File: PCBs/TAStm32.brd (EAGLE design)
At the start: 45 x 68.1 mm, 23 parts, among them J1 ZX62D-B-5PA8, P1 RJHSE-5381, P1_DEBUG 6_PIN_SERIAL_CABLEPTH, P2 RJHSE-5381, P2_DEBUG 6_PIN_SERIAL_CABLEPTH, U1 STM32F446RET6

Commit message: updated PCBs to v1
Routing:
- net N$3: track 19.8 -> 17.4 mm, vias 2 -> 0
- net V2_D0: track 27.0 -> 29.3 mm
- net V2_LATCH: track 31.2 -> 33.4 mm
- net V2_CLOCK: track 33.5 -> 35.5 mm
- net V2_D1: track 30.7 -> 32.7 mm
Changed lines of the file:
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@@
 <text x="14.3" y="20.4" size="0.6096" layer="25" font="vector" ratio="15" rot="R180">SWITCH</text>
 <text x="10" y="34" size="0.6096" layer="25" font="vector" ratio="15">V_REG</text>
-<text x="28.9" y="25.7" size="0.6096" layer="26" font="vector" ratio="15" rot="MR0">Hardware design by:
+<text x="24.9" y="21.7" size="0.6096" layer="26" font="vector" ratio="15" rot="MR0">Hardware design by:
 Ownasaurus
 https://github.com/Ownasaurus/TAStm32</text>
@@
 <contactref element="R2" pad="2"/>
 <contactref element="SWITCH" pad="P$2"/>
-<wire x1="17.24" y1="20.03" x2="20" y2="20.03" width="0.1524" layer="1"/>
-<wire x1="20" y1="20.03" x2="20" y2="20" width="0.1524" layer="1"/>
-<via x="20" y="20" extent="1-16" drill="0.35"/>
-<wire x1="20" y1="20" x2="20" y2="23" width="0.1524" layer="16"/>
-<via x="20" y="23" extent="1-16" drill="0.35"/>
-<wire x1="20" y1="23" x2="18.17" y2="24.83" width="0.1524" layer="1"/>
-<wire x1="18.17" y1="24.83" x2="17.47" y2="24.83" width="0.1524" layer="1"/>
-<wire x1="28.8786" y1="24.93368125" x2="28.70368125" y2="25.1086" width="0.1524" layer="1"/>
+<wire x1="28.70368125" y1="25.1086" x2="28.8786" y2="24.93368125" width="0.1524" layer="1"/>
 <wire x1="29.01" y1="24.1" x2="28.8786" y2="24.2314" width="0.1524" layer="1"/>
 <wire x1="28.8786" y1="24.2314" x2="28.8786" y2="24.93368125" width="0.1524" layer="1"/>
-<wire x1="28.70368125" y1="25.1086" x2="22.1086" y2="25.1086" width="0.1524" layer="1"/>
-<wire x1="22.1086" y1="25.1086" x2="20" y2="23" width="0.1524" layer="1"/>
+<wire x1="17.24" y1="20.03" x2="17.24" y2="24.6" width="0.1524" layer="1"/>
+<wire x1="17.24" y1="24.6" x2="17.47" y2="24.83" width="0.1524" layer="1"/>
+<wire x1="17.47" y1="24.83" x2="17.7486" y2="25.1086" width="0.1524" layer="1"/>
+<wire x1="17.7486" y1="25.1086" x2="28.70368125" y2="25.1086" width="0.1524" layer="1"/>
 </signal>
 <signal name="N$4">
@@
 <wire x1="5.0436" y1="10.7657125" x2="5" y2="10.7221125" width="0.1524" layer="1"/>
 <wire x1="5" y1="10.7221125" x2="5" y2="8.76" width="0.1524" layer="1"/>
-<wire x1="24.01" y1="24.1" x2="23.8786" y2="23.9686" width="0.1524" layer="1"/>
-<wire x1="23.8786" y1="23.9686" x2="23.8786" y2="23.26631875" width="0.1524" layer="1"/>
-<wire x1="23.8786" y1="23.26631875" x2="22.61228125" y2="22" width="0.1524" layer="1"/>
-<wire x1="22.61228125" y1="22" x2="15" y2="22" width="0.1524" layer="1"/>
-<wire x1="15" y1="22" x2="11" y2="18" width="0.1524" layer="1"/>
-<wire x1="11" y1="18" x2="7" y2="18" width="0.1524" layer="1"/>
-<wire x1="7" y1="18" x2="5" y2="16" width="0.1524" layer="1"/>
-<wire x1="5" y1="16" x2="5" y2="15" width="0.1524" layer="1"/>
+<wire x1="5" y1="15" x2="8.3048" y2="18.3048" width="0.1524" layer="1"/>
+<wire x1="8.3048" y1="18.3048" x2="23.4" y2="18.3048" width="0.1524" layer="1"/>
+<wire x1="23.4" y1="18.3048" x2="24.01" y2="18.9148" width="0.1524" layer="1"/>
+<wire x1="24.01" y1="18.9148" x2="24.01" y2="24.1" width="0.1524" layer="1"/>
 </signal>
 <signal name="V2_LATCH">
@@
 <wire x1="7.54" y1="15" x2="7.54" y2="8.25" width="0.1524" layer="1"/>
 <wire x1="7.54" y1="8.25" x2="9.47" y2="6.32" width="0.1524" layer="1"/>
-<wire x1="7.54" y1="15" x2="9.54" y2="17" width="0.1524" layer="1"/>
-<wire x1="9.54" y1="17" x2="12" y2="17" width="0.1524" layer="1"/>
-<wire x1="12" y1="17" x2="16" y2="21" width="0.1524" layer="1"/>
-<wire x1="16" y1="21" x2="23" y2="21" width="0.1524" layer="1"/>
-<wire x1="23" y1="21" x2="24.51" y2="22.51" width="0.1524" layer="1"/>
-<wire x1="24.51" y1="22.51" x2="24.51" y2="24.1" width="0.1524" layer="1"/>
+<wire x1="7.54" y1="15" x2="10.54" y2="18" width="0.1524" layer="1"/>
+<wire x1="10.54" y1="18" x2="23.9" y2="18" width="0.1524" layer="1"/>
+<wire x1="23.9" y1="18" x2="24.51" y2="18.61" width="0.1524" layer="1"/>
+<wire x1="24.51" y1="18.61" x2="24.51" y2="24.1" width="0.1524" layer="1"/>
 </signal>
 <signal name="V2_D1">
@@
 <wire x1="10.49" y1="4.54" x2="10.49" y2="14.59" width="0.1524" layer="1"/>
 <wire x1="10.49" y1="14.59" x2="10.08" y2="15" width="0.1524" layer="1"/>
-<wire x1="25.01" y1="24.1" x2="25" y2="24.09" width="0.1524" layer="1"/>
-<wire x1="25" y1="24.09" x2="25" y2="22" width="0.1524" layer="1"/>
-<wire x1="25" y1="22" x2="22" y2="19" width="0.1524" layer="1"/>
-<wire x1="12.4" y1="16.4" x2="11.2" y2="16.4" width="0.1524" layer="1"/>
-<wire x1="11.2" y1="16.4" x2="10.08" y2="15.28" width="0.1524" layer="1"/>
-<wire x1="10.08" y1="15.28" x2="10.08" y2="15" width="0.1524" layer="1"/>
-<wire x1="22" y1="19" x2="15" y2="19" width="0.1524" layer="1"/>
-<wire x1="15" y1="19" x2="12.4" y2="16.4" width="0.1524" layer="1"/>
+<wire x1="25" y1="24.09" x2="25.01" y2="24.1" width="0.1524" layer="1"/>
+<wire x1="10.08" y1="15" x2="12.3848" y2="17.3048" width="0.1524" layer="1"/>
+<wire x1="12.3848" y1="17.3048" x2="24" y2="17.3048" width="0.1524" layer="1"/>
+<wire x1="24" y1="17.3048" x2="25" y2="18.3048" width="0.1524" layer="1"/>
+<wire x1="25" y1="18.3048" x2="25" y2="24.09" width="0.1524" layer="1"/>
 </signal>
 <signal name="V2_D0">
@@
 <wire x1="11.5" y1="6.32" x2="11.5" y2="13.88" width="0.1524" layer="1"/>
 <wire x1="11.5" y1="13.88" x2="12.62" y2="15" width="0.1524" layer="1"/>
-<wire x1="12.62" y1="15" x2="16.3152" y2="18.6952" width="0.1524" layer="1"/>
-<wire x1="16.3152" y1="18.6952" x2="22.12625625" y2="18.6952" width="0.1524" layer="1"/>
-<wire x1="25.3786" y1="23.9686" x2="25.51" y2="24.1" width="0.1524" layer="1"/>
-<wire x1="22.12625625" y1="18.6952" x2="25.3786" y2="21.94754375" width="0.1524" layer="1"/>
-<wire x1="25.3786" y1="21.94754375" x2="25.3786" y2="23.9686" width="0.1524" layer="1"/>
+<wire x1="12.62" y1="15" x2="14.62" y2="17" width="0.1524" layer="1"/>
+<wire x1="14.62" y1="17" x2="24.4" y2="17" width="0.1524" layer="1"/>
+<wire x1="24.4" y1="17" x2="25.51" y2="18.11" width="0.1524" layer="1"/>
+<wire x1="25.51" y1="18.11" x2="25.51" y2="24.1" width="0.1524" layer="1"/>
 </signal>
 <signal name="V1_CLOCK">

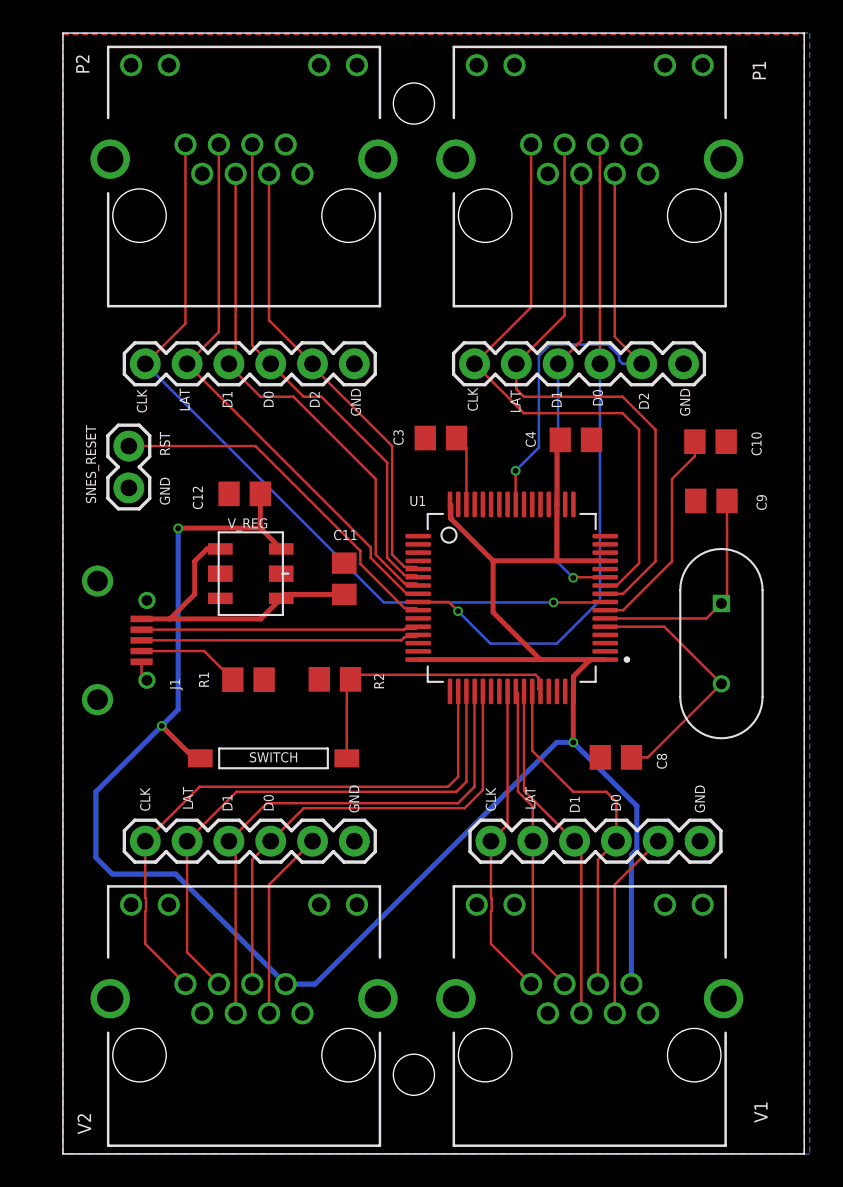
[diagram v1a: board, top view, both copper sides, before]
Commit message: works with new pin assignments
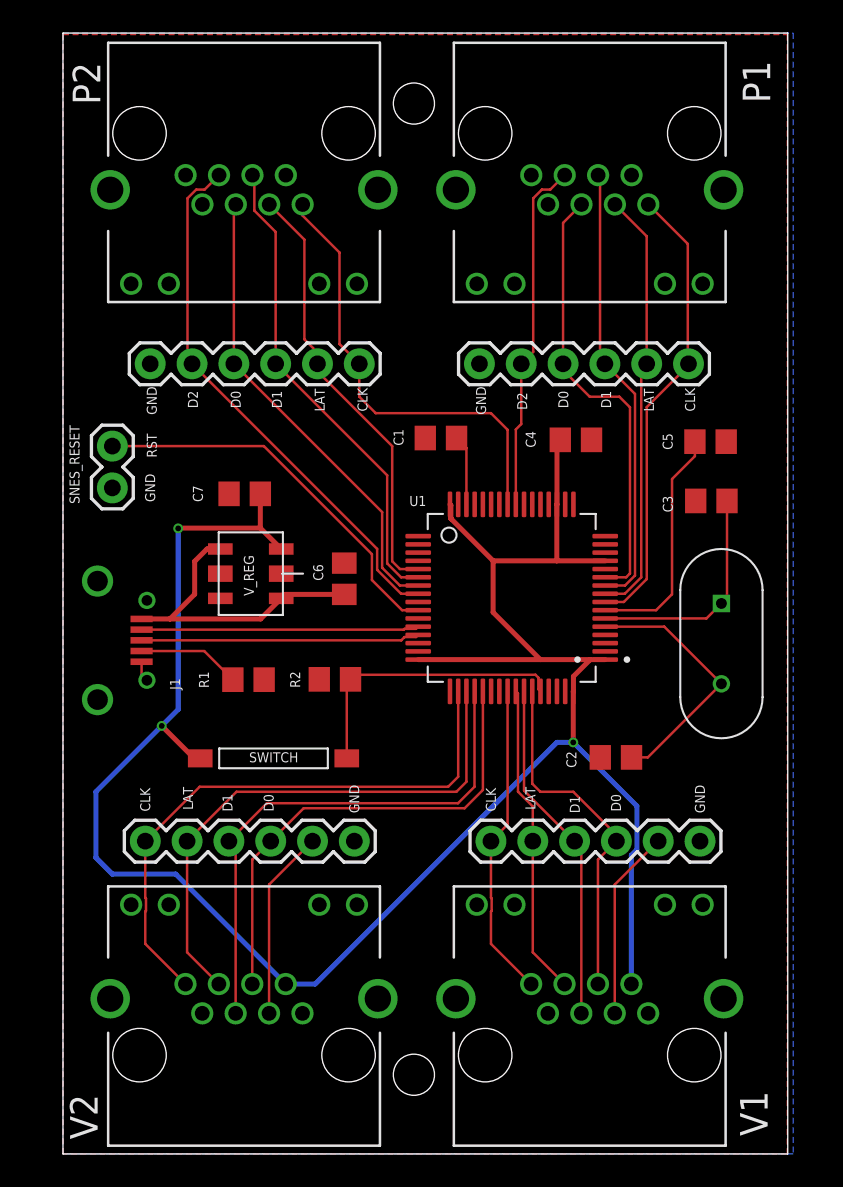
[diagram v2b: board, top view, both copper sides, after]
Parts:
- removed C9: 25pF, eagle-ltspice:C0805
- added C1: 4.7uF, eagle-ltspice:C0805
- C3: value 4.7uF -> 25pF
- moved C3 16.9 mm to (39.4, 35.7), turned to 0 degrees
- moved P1_DEBUG 13.0 mm to (38.0, 44.0), turned to 180 degrees
- moved P2_DEBUG 13.0 mm to (18.0, 44.0), turned to 180 degrees
- moved P1 5.00 mm to (32.0, 58.0), turned to 180 degrees
- moved P2 5.00 mm to (11.0, 58.0), turned to 180 degrees
- moved SNES_RESET 1.00 mm to (3.00, 39.0)
- renumbered C10 to C5, C11 to C6, C12 to C7, C8 to C2
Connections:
- net GND: now also C1.2, C3.1; no longer C3.2, C9.1
- net N$6: now also C1.1; no longer C3.1
- net P1_CLOCK: now also U1.8; no longer U1.10
- net P1_D0: now also U1.11; no longer U1.41
- net P1_D1: now also U1.10; no longer U1.11
- net P2_CLOCK: now also U1.25; no longer U1.8
- net P2_D0: now also U1.39; no longer U1.38
- net P2_D1: now also U1.38; no longer U1.39
- net P2_D2: now also U1.40; no longer U1.37
- net P2_LATCH: now also U1.37; no longer U1.40
- net XTAL2: now also C3.2; no longer C9.2
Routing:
- net P2_CLOCK: track 48.3 -> 27.5 mm, vias 1 -> 0
- net P1_D0: track 40.9 -> 27.2 mm, vias 1 -> 0
- net P1_LATCH: track 37.4 -> 26.2 mm
- net P1_CLOCK: track 37.1 -> 27.9 mm
- net P2_LATCH: track 34.3 -> 26.5 mm
- net P1_D2: track 29.0 -> 21.5 mm, vias 1 -> 0
- net P2_D2: track 28.3 -> 32.9 mm
- net P2_D0: track 31.5 -> 28.5 mm
- net P2_D1: track 31.5 -> 29.2 mm
- net SNES_RESET: track 22.2 -> 23.6 mm
- net N$4: track 13.1 -> 14.3 mm
- net P1_D1: track 27.5 -> 27.3 mm, vias 1 -> 0
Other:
- board size 45 x 68.1 mm -> 44 x 68.1 mm
- board text added: "Hardware design by: Ownasaurus TheMas3212 https://github.com/Ownasaurus/TAStm32"
- board text removed: "Hardware design by: Ownasaurus https://github.com/Ownasaurus/TAStm32"
